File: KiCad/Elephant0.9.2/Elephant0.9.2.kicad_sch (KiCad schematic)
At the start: 48 parts, among them J1 Conn_01x04_Pin, J2 Conn_01x05_Pin, SW1 SW_TILT, U1 LT8640, U3 SSM2518, U4 M95M04, U5 STM32F401CCUx, Y1 32.768kHz, 6pF, 50kΩ, Y2 16MHz, 7pF, 60Ω

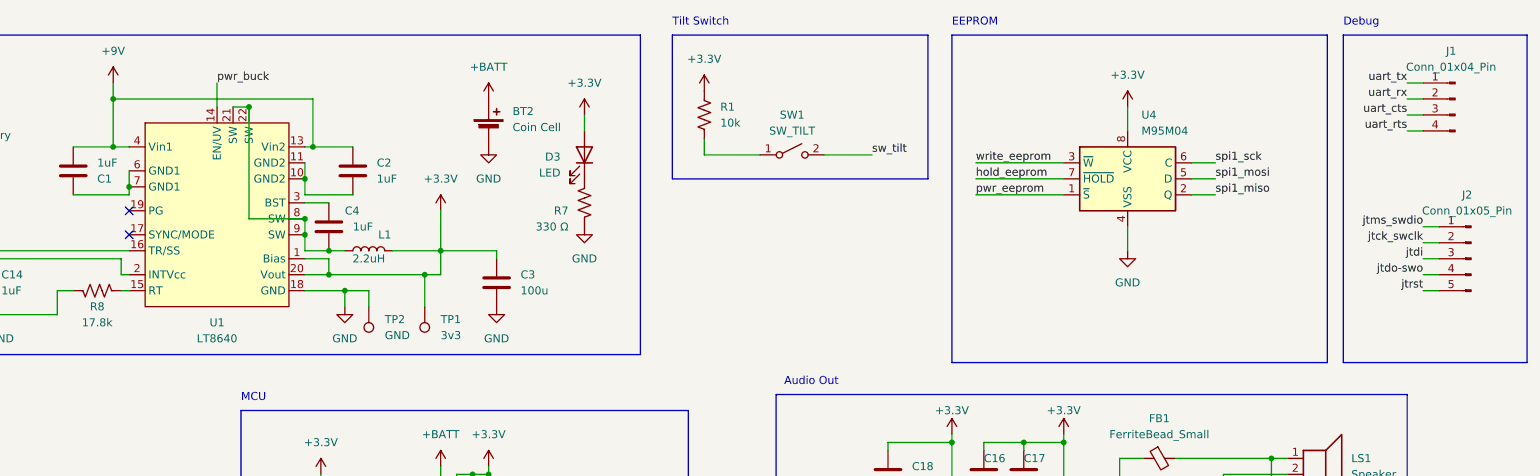
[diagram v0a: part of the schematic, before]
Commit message: Added the audio system with a way to test it.
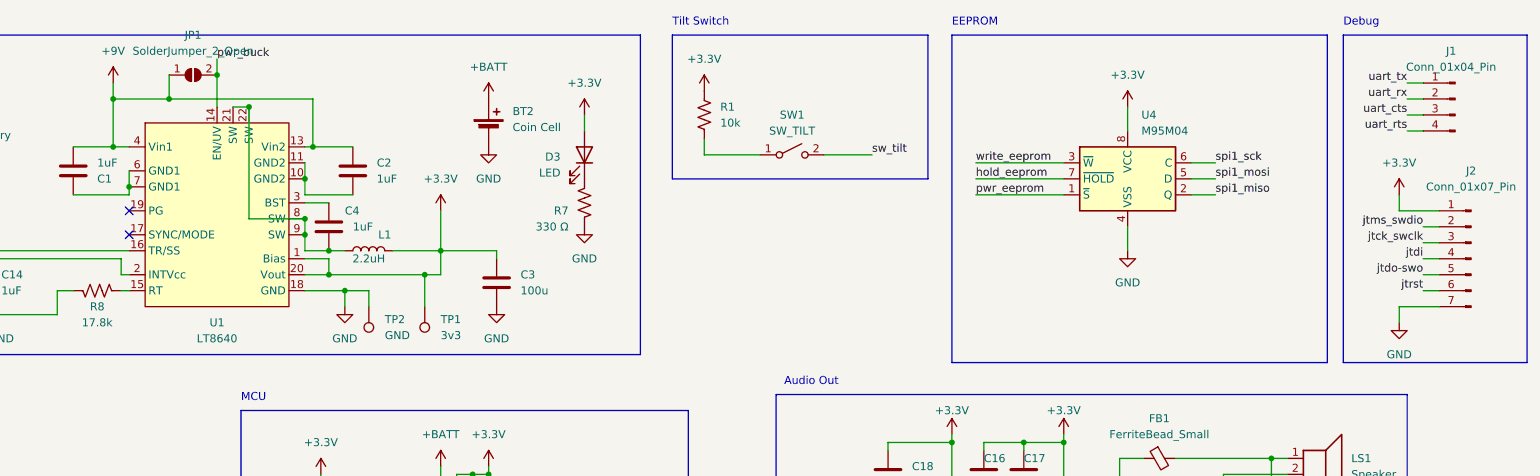
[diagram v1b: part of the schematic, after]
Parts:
- added JP1: SolderJumper_2_Open, Jumper:SolderJumper-2_P1.3mm_Open_Pad1.0x1.5mm, symbol Jumper:SolderJumper_2_Open
- C11, C12, C13, C15, C16, C18, C5, C6, C7, C8, C9: footprint Capacitor_SMD:C_0201_0603Metric -> Capacitor_SMD:C_0603_1608Metric
- J2: value Conn_01x05_Pin -> Conn_01x07_Pin; footprint Connector_JST:JST_PH_B5B-PH-K_1x05_P2.00mm_Vertical -> Connector_JST:JST_PH_B7B-PH-K_1x07_P2.00mm_Vertical; symbol Connector:Conn_01x05_Pin -> Connector:Conn_01x07_Pin
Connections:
- net +3.3V: now also J2.1 (Pin_1)
- net +9V: now also JP1.1 (A)
- net GND: now also J2.7 (Pin_7)
- net jtck_swclk: now also J2.3 (Pin_3); no longer J2.2 (Pin_2)
- net jtdi: now also J2.4 (Pin_4); no longer J2.3 (Pin_3)
- net jtdo-swo: now also J2.5 (Pin_5); no longer J2.4 (Pin_4)
- net jtms_swdio: now also J2.2 (Pin_2); no longer J2.1 (Pin_1)
- net jtrst: now also J2.6 (Pin_6); no longer J2.5 (Pin_5)
- net pwr_buck: now also JP1.2 (B)
